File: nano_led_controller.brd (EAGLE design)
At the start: 40.7 x 47 mm, 9 parts, among them X1 JST-XH-03-PIN-LONG-PAD, X2 JST-XH-04-PIN-LONG-PAD

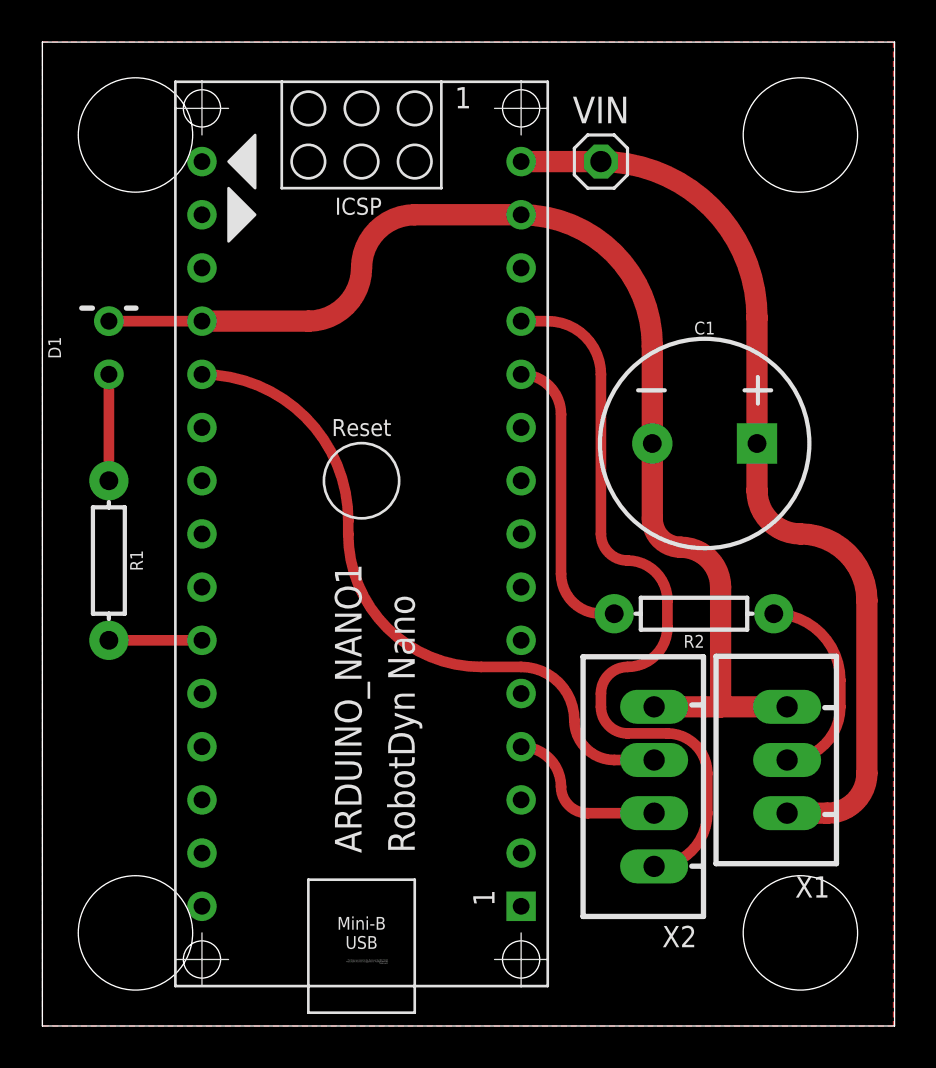
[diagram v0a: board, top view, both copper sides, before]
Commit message: Rearranged board to work with right angle USB cable
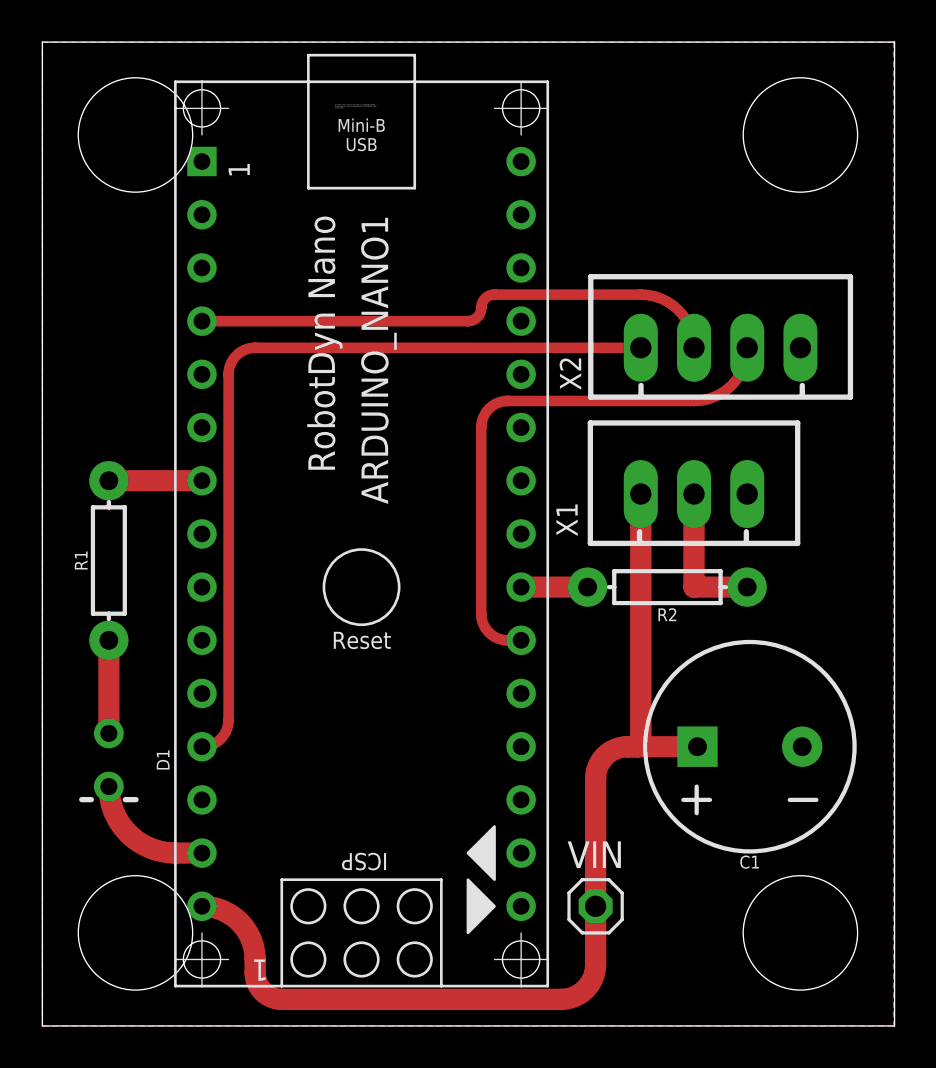
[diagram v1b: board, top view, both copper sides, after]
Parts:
- moved VIN 35.6 mm to (25.1, 4.45)
- moved X2 21.2 mm to (31.1, 31.1), turned to 0 degrees
- moved D1 19.7 mm to (1.91, 11.4), turned to 270 degrees
- moved C1 14.6 mm to (32.5, 12.1), turned to 180 degrees
- moved X1 13.5 mm to (29.8, 24.1), turned to 0 degrees
- moved ARDUINO_NANO1 5.08 mm to (14.0, 19.7), turned to 270 degrees
- moved R2 1.80 mm to (28.6, 19.7)
- turned R1 to 90 degrees
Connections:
- net N$3 renamed ADC
- removed net N$7: ARDUINO_NANO1.25, R1.P$2
- new net N$3: ARDUINO_NANO1.22, R2.P$2
- net N$1: now also ARDUINO_NANO1.7, R1.P$2; no longer ARDUINO_NANO1.11, R2.P$2
- net N$6: now also ARDUINO_NANO1.21; no longer ARDUINO_NANO1.20
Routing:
- net GND: track 55.6 -> 5.76 mm
- net ADC: track 7.67 -> 25.1 mm
- net N$1: track 13.6 -> 4.44 mm
- net VIN: track 42.9 -> 48.7 mm
- net N$7: track 4.44 -> 0.00 mm
- net N$6: track 29.6 -> 25.6 mm
- net 5V: track 35.3 -> 38.5 mm
- net N$3: track 0.00 -> 3.18 mm
- net N$2: track 9.35 -> 6.98 mm
- net N$4: track 5.08 -> 4.45 mm

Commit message: 50mil traces and more ground plane Pins 16(D1/TX),26(D8/CLK0),27(D9/OC1A) are out of commission.
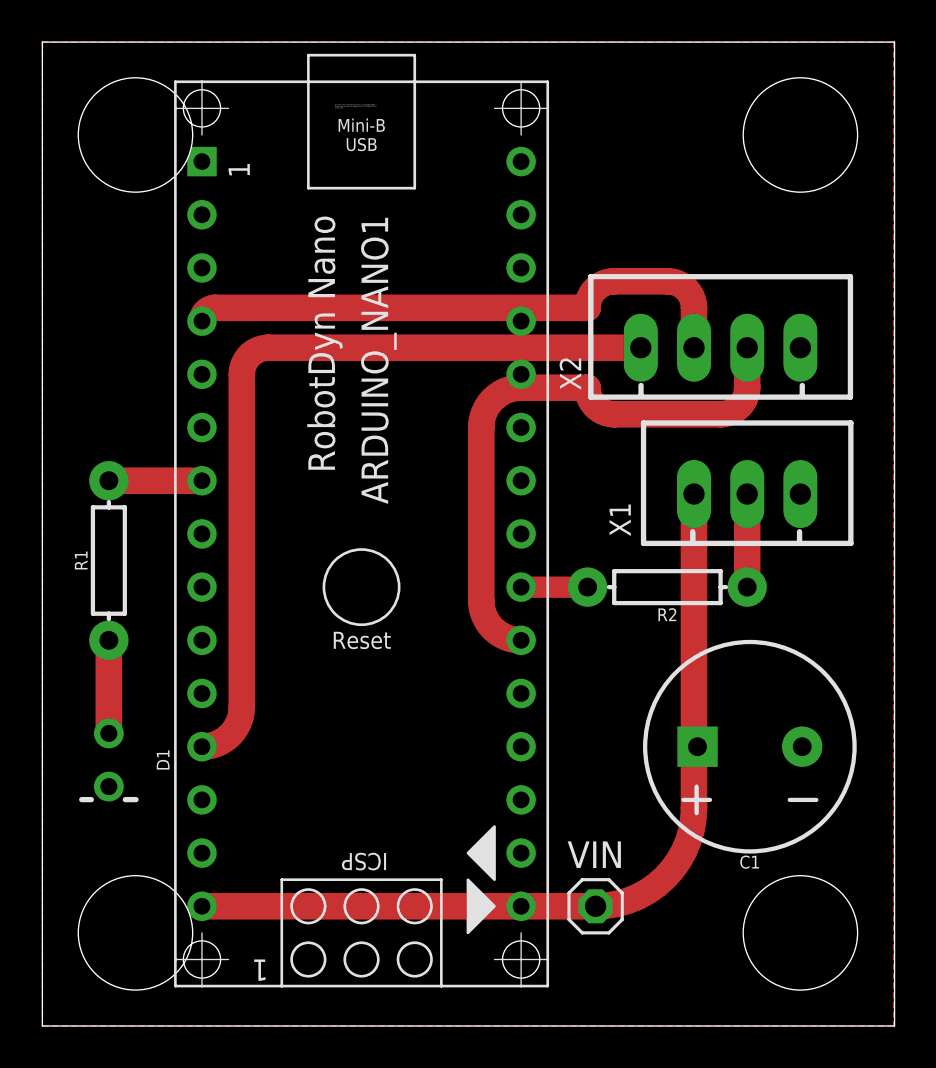
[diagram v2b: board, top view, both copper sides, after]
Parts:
- moved X1 2.54 mm to (32.4, 24.1)
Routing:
- net VIN: track 48.7 -> 40.6 mm
- net GND: track 5.76 -> 0.00 mm
- net N$2: track 6.98 -> 4.45 mm
- net N$6: track 25.6 -> 27.4 mm
- net ADC: track 25.1 -> 26.7 mm
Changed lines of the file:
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@@
 </element>
 <element name="VIN" library="pinhead" library_urn="urn:adsk.eagle:library:325" package="1X01" value="USB VIN" x="25.146" y="4.445"/>
-<element name="X1" library="Rembrandt Electronics - JST XH Connectors v1-0" package="JST-XH-03-PACKAGE-LONG-PAD" value="JST-XH-03-PIN-LONG-PAD" x="29.845" y="24.13"/>
+<element name="X1" library="Rembrandt Electronics - JST XH Connectors v1-0" package="JST-XH-03-PACKAGE-LONG-PAD" value="JST-XH-03-PIN-LONG-PAD" x="32.385" y="24.13"/>
 <element name="X2" library="Rembrandt Electronics - JST XH Connectors v1-0" package="JST-XH-04-PACKAGE-LONG-PAD" value="JST-XH-04-PIN-LONG-PAD" x="31.115" y="31.115"/>
 <element name="D1" library="SparkFun-LED" package="LED_3MM-NS" value="Power LED" x="1.905" y="11.43" rot="R270"/>
@@
 </polygon>
 <contactref element="ARDUINO_NANO1" pad="14"/>
-<wire x1="6.35" y1="6.985" x2="5.08" y2="6.985" width="1.016" layer="1"/>
-<wire x1="5.08" y1="6.985" x2="1.905" y2="10.16" width="1.016" layer="1" curve="-90"/>
 </signal>
 <signal name="VIN">
@@
 <contactref element="X1" pad="1"/>
 <contactref element="ARDUINO_NANO1" pad="15"/>
-<wire x1="6.35" y1="4.445" x2="8.89" y2="1.905" width="1.016" layer="1" curve="-90"/>
-<wire x1="8.89" y1="1.905" x2="8.89" y2="1.27" width="1.016" layer="1"/>
-<wire x1="8.89" y1="1.27" x2="10.16" y2="0" width="1.016" layer="1" curve="90"/>
-<wire x1="10.16" y1="0" x2="23.495" y2="0" width="1.016" layer="1"/>
-<wire x1="23.495" y1="0" x2="25.146" y2="1.651" width="1.016" layer="1" curve="90"/>
-<wire x1="25.146" y1="1.651" x2="25.146" y2="4.445" width="1.016" layer="1"/>
-<wire x1="27.305" y1="24.13" x2="27.305" y2="12.192" width="1.016" layer="1"/>
-<wire x1="25.146" y1="4.445" x2="25.146" y2="10.541" width="1.016" layer="1"/>
-<wire x1="26.67" y1="12.065" x2="25.146" y2="10.541" width="1.016" layer="1" curve="90"/>
-<wire x1="26.67" y1="12.065" x2="27.178" y2="12.065" width="1.016" layer="1"/>
-<wire x1="27.178" y1="12.065" x2="27.305" y2="12.192" width="1.016" layer="1" curve="90"/>
-<wire x1="30.012" y1="12.065" x2="26.67" y2="12.065" width="1.016" layer="1"/>
+<wire x1="29.845" y1="12.065" x2="30.012" y2="12.065" width="1.27" layer="1"/>
+<wire x1="29.845" y1="12.065" x2="29.845" y2="24.13" width="1.27" layer="1"/>
+<wire x1="6.35" y1="4.445" x2="25.146" y2="4.445" width="1.27" layer="1"/>
+<wire x1="25.146" y1="4.445" x2="29.845" y2="9.144" width="1.27" layer="1" curve="90"/>
+<wire x1="29.845" y1="9.144" x2="29.845" y2="12.065" width="1.27" layer="1"/>
 </signal>
 <signal name="N$5">
@@
 <contactref element="R2" pad="P$1"/>
 <contactref element="X1" pad="2"/>
-<wire x1="29.845" y1="24.13" x2="29.845" y2="19.685" width="1.016" layer="1"/>
-<wire x1="29.845" y1="19.685" x2="32.385" y2="19.685" width="1.016" layer="1"/>
+<wire x1="32.385" y1="19.685" x2="32.385" y2="24.13" width="1.27" layer="1"/>
 </signal>
 <signal name="N$4">
 <contactref element="D1" pad="A"/>
 <contactref element="R1" pad="P$1"/>
-<wire x1="1.905" y1="17.145" x2="1.905" y2="12.7" width="1.016" layer="1"/>
+<wire x1="1.905" y1="12.7" x2="1.905" y2="17.145" width="1.27" layer="1"/>
 </signal>
 <signal name="N$1">
 <contactref element="R1" pad="P$2"/>
 <contactref element="ARDUINO_NANO1" pad="7"/>
-<wire x1="6.35" y1="24.765" x2="1.905" y2="24.765" width="1.016" layer="1"/>
+<wire x1="1.905" y1="24.765" x2="6.35" y2="24.765" width="1.27" layer="1"/>
 </signal>
 <signal name="N$3">
@@
 <contactref element="X2" pad="3"/>
 <contactref element="ARDUINO_NANO1" pad="21"/>
-<wire x1="32.385" y1="31.115" x2="29.845" y2="28.575" width="0.508" layer="1" curve="-90"/>
-<wire x1="29.845" y1="28.575" x2="20.955" y2="28.575" width="0.508" layer="1"/>
-<wire x1="20.955" y1="28.575" x2="19.685" y2="27.305" width="0.508" layer="1" curve="90"/>
-<wire x1="19.685" y1="27.305" x2="19.685" y2="18.415" width="0.508" layer="1"/>
-<wire x1="19.685" y1="18.415" x2="20.955" y2="17.145" width="0.508" layer="1" curve="90"/>
-<wire x1="20.955" y1="17.145" x2="21.59" y2="17.145" width="0.508" layer="1"/>
+<wire x1="21.59" y1="17.145" x2="19.685" y2="19.05" width="1.27" layer="1" curve="-90"/>
+<wire x1="19.685" y1="19.05" x2="19.685" y2="27.305" width="1.27" layer="1"/>
+<wire x1="19.685" y1="27.305" x2="21.59" y2="29.21" width="1.27" layer="1" curve="-90"/>
+<wire x1="21.59" y1="29.21" x2="24.765" y2="29.21" width="1.27" layer="1"/>
+<wire x1="24.765" y1="29.21" x2="26.035" y2="27.94" width="1.27" layer="1" curve="90"/>
+<wire x1="26.035" y1="27.94" x2="31.115" y2="27.94" width="1.27" layer="1"/>
+<wire x1="31.115" y1="27.94" x2="32.385" y2="29.21" width="1.27" layer="1" curve="90"/>
+<wire x1="32.385" y1="29.21" x2="32.385" y2="31.115" width="1.27" layer="1"/>
 </signal>
 <signal name="ADC">
 <contactref element="X2" pad="2"/>
 <contactref element="ARDUINO_NANO1" pad="4"/>
-<wire x1="29.845" y1="31.115" x2="27.305" y2="33.655" width="0.508" layer="1" curve="90"/>
-<wire x1="20.32" y1="33.655" x2="19.685" y2="33.02" width="0.508" layer="1" curve="90"/>
-<wire x1="19.685" y1="33.02" x2="19.05" y2="32.385" width="0.508" layer="1" curve="-90"/>
-<wire x1="19.05" y1="32.385" x2="6.35" y2="32.385" width="0.508" layer="1"/>
-<wire x1="27.305" y1="33.655" x2="20.32" y2="33.655" width="0.508" layer="1"/>
+<wire x1="6.35" y1="32.385" x2="6.985" y2="33.02" width="1.27" layer="1" curve="-90"/>
+<wire x1="24.765" y1="33.02" x2="6.985" y2="33.02" width="1.27" layer="1"/>
+<wire x1="29.845" y1="31.115" x2="29.845" y2="33.02" width="1.27" layer="1"/>
+<wire x1="29.845" y1="33.02" x2="28.575" y2="34.29" width="1.27" layer="1" curve="90"/>
+<wire x1="28.575" y1="34.29" x2="26.035" y2="34.29" width="1.27" layer="1"/>
+<wire x1="26.035" y1="34.29" x2="24.765" y2="33.02" width="1.27" layer="1" curve="90"/>
 </signal>
 <signal name="5V">
 <contactref element="ARDUINO_NANO1" pad="12"/>
 <contactref element="X2" pad="1"/>
-<wire x1="27.305" y1="31.115" x2="8.89" y2="31.115" width="0.508" layer="1"/>
-<wire x1="8.89" y1="31.115" x2="7.62" y2="29.845" width="0.508" layer="1" curve="90"/>
-<wire x1="7.62" y1="13.335" x2="6.35" y2="12.065" width="0.508" layer="1" curve="-90"/>
-<wire x1="7.62" y1="29.845" x2="7.62" y2="13.335" width="0.508" layer="1"/>
+<wire x1="6.35" y1="12.065" x2="8.255" y2="13.97" width="1.27" layer="1" curve="90"/>
+<wire x1="8.255" y1="29.845" x2="9.525" y2="31.115" width="1.27" layer="1" curve="-90"/>
+<wire x1="9.525" y1="31.115" x2="27.305" y2="31.115" width="1.27" layer="1"/>
+<wire x1="8.255" y1="13.97" x2="8.255" y2="29.845" width="1.27" layer="1"/>
 </signal>
 </signals>
